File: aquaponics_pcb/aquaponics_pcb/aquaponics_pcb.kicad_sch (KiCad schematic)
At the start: 0 parts

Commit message: initial commit with kicad project
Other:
- added sheet ESP32_MCU (ESP32_MCU.kicad_sch)
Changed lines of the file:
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@@
+		)
+	)
+	(sheet
+		(at 106.68 76.2)
+		(size 29.21 19.05)
+		(exclude_from_sim no)
+		(in_bom yes)
+		(on_board yes)
+		(dnp no)
+		(fields_autoplaced yes)
+		(stroke
+			(width 0.1524)
+			(type solid)
+		)
+		(fill
+			(color 0 0 0 0.0000)
+		)
+		(property "Sheetname" "ESP32_MCU"
+			(at 106.68 75.4884 0)
+			(effects
+				(font
+					(size 1.27 1.27)
+				)
+				(justify left bottom)
+			)
+		)
+		(property "Sheetfile" "ESP32_MCU.kicad_sch"
+			(at 106.68 95.8346 0)
+			(effects
+				(font
+					(size 1.27 1.27)
+				)
+				(justify left top)
+			)
+		)
+		(instances
+			(project "aquaponics_pcb"
+				(path "/c5e5a8d2-0dcc-4520-98a5-511e1dc0d12f"
+					(page "3")
+				)
+			)
 		)
 	)

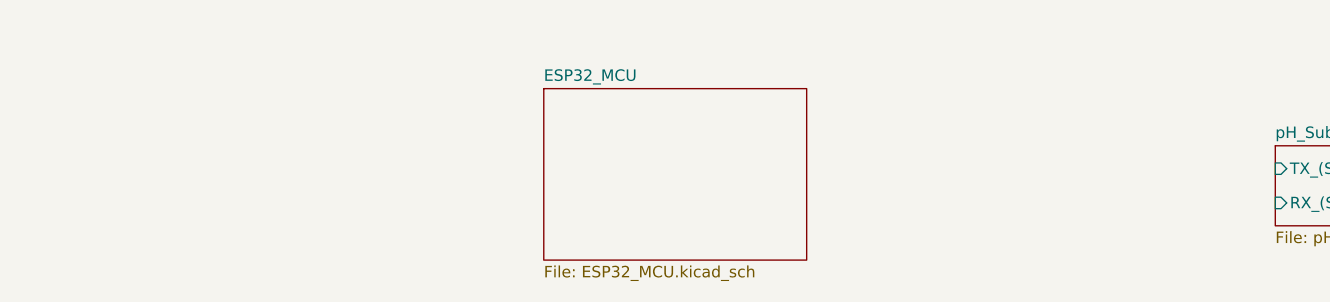
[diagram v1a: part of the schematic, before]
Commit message: finish MCU and start logic isolation block
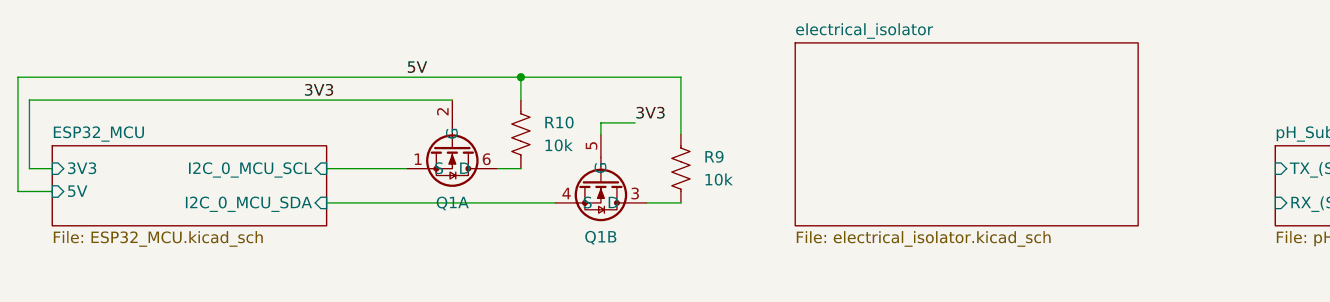
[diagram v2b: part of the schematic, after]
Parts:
- added Q1: SSM6N35AFE,LF, SOTFL50P160X60-6N, symbol SamacSys_Parts:SSM6N35AFE,LF
- added R10, R9: 10k, Resistor_SMD:R_0603_1608Metric_Pad0.98x0.95mm_HandSolder, symbol Device:R_US
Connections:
- new net: Q1.3 (D), R9.1
- new net: Q1.6 (D), R10.1
- new net 3V3: Q1.2 (G), Q1.5 (G)
- new net 5V: R10.2, R9.2
- new net ESP32_MCU/I2C_0_MCU_SCL: Q1.1 (S)
- new net ESP32_MCU/I2C_0_MCU_SDA: Q1.4 (S)
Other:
- added sheet electrical_isolator (electrical_isolator.kicad_sch)
- sheet ESP32_MCU ports: added 3V3, 5V, I2C_0_MCU_SCL, I2C_0_MCU_SDA; removed none

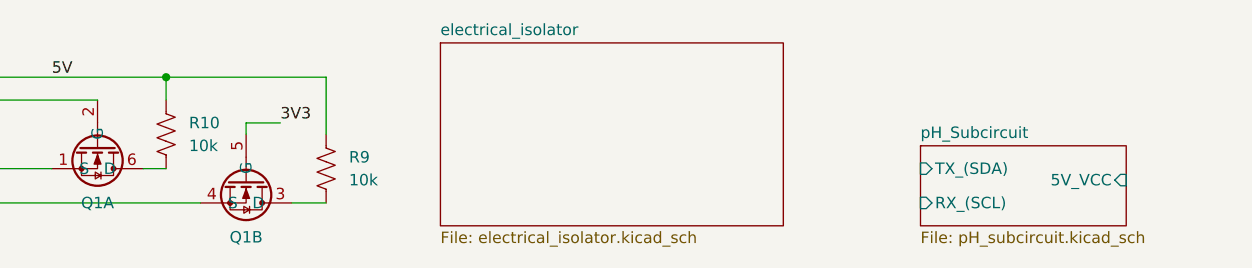
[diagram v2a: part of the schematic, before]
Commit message: update isolator circuit
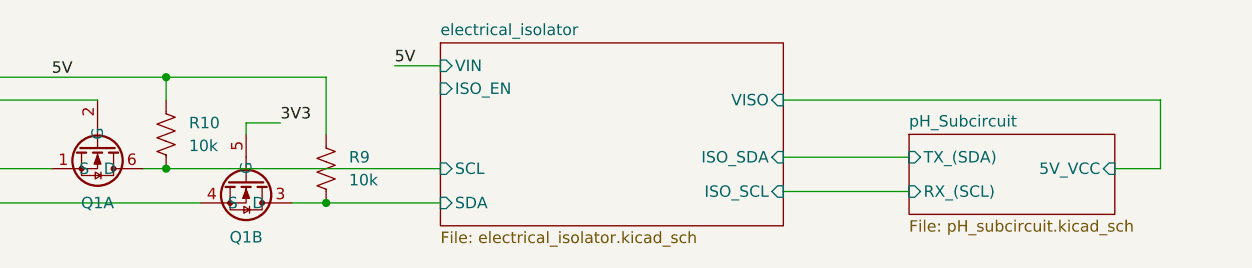
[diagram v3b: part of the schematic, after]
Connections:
- net electrical_isolator/SDA: now reaches Q1.3 (D), R9.1
- net electrical_isolator/SCL: now reaches Q1.6 (D), R10.1
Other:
- sheet electrical_isolator ports: added ISO_EN, ISO_SCL, ISO_SDA, SCL, SDA, VIN, VISO; removed none
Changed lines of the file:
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@@
 	(paper "A4")
+	(junction
+		(at 104.14 85.09)
+		(diameter 0)
+		(color 0 0 0 0)
+	)
+	(junction
+		(at 121.92 88.9)
+		(diameter 0)
+		(color 0 0 0 0)
+	)
 	(junction
 		(at 104.14 74.93)
@@
 	(wire
 		(pts
+			(xy 172.72 83.82) (xy 186.69 83.82)
+		)
+		(stroke
+			(width 0)
+			(type default)
+		)
+	)
+	(wire
+		(pts
+			(xy 172.72 77.47) (xy 214.63 77.47)
+		)
+		(stroke
+			(width 0)
+			(type default)
+		)
+	)
+	(wire
+		(pts
 			(xy 118.11 88.9) (xy 121.92 88.9)
 		)
@@
 	(wire
 		(pts
+			(xy 214.63 77.47) (xy 214.63 85.09)
+		)
+		(stroke
+			(width 0)
+			(type default)
+		)
+	)
+	(wire
+		(pts
+			(xy 214.63 85.09) (xy 209.55 85.09)
+		)
+		(stroke
+			(width 0)
+			(type default)
+		)
+	)
+	(wire
+		(pts
+			(xy 129.54 73.66) (xy 134.62 73.66)
+		)
+		(stroke
+			(width 0)
+			(type default)
+		)
+	)
+	(wire
+		(pts
 			(xy 101.6 85.09) (xy 104.14 85.09)
 		)
@@
 	(wire
 		(pts
+			(xy 104.14 85.09) (xy 134.62 85.09)
+		)
+		(stroke
+			(width 0)
+			(type default)
+		)
+	)
+	(wire
+		(pts
+			(xy 121.92 88.9) (xy 134.62 88.9)
+		)
+		(stroke
+			(width 0)
+			(type default)
+		)
+	)
+	(wire
+		(pts
 			(xy 49.53 77.47) (xy 96.52 77.47)
 		)
@@
 		(pts
 			(xy 104.14 74.93) (xy 104.14 77.47)
+		)
+		(stroke
+			(width 0)
+			(type default)
+		)
+	)
+	(wire
+		(pts
+			(xy 172.72 87.63) (xy 186.69 87.63)
 		)
 		(stroke
@@
 	(label "5V"
 		(at 91.44 74.93 0)
+		(effects
+			(font
+				(size 1.27 1.27)
+			)
+			(justify left bottom)
+		)
+	)
+	(label "5V"
+		(at 129.54 73.66 0)
 		(effects
 			(font
@@
 	)
 	(sheet
-		(at 187.96 82.55)
+		(at 186.69 81.28)
 		(size 22.86 8.89)
 		(exclude_from_sim no)
@@
 		)
 		(property "Sheetname" "pH_Subcircuit"
-			(at 187.96 81.8384 0)
+			(at 186.69 80.5684 0)
 			(effects
 				(font
@@
 		)
 		(property "Sheetfile" "pH_subcircuit.kicad_sch"
-			(at 187.96 92.0246 0)
+			(at 186.69 90.7546 0)
 			(effects
 				(font
@@
 		)
 		(pin "TX_(SDA)" input
-			(at 187.96 85.09 180)
+			(at 186.69 83.82 180)
 			(effects
 				(font
@@
 		)
 		(pin "5V_VCC" input
-			(at 210.82 86.36 0)
+			(at 209.55 85.09 0)
 			(effects
 				(font
@@
 		)
 		(pin "RX_(SCL)" input
-			(at 187.96 88.9 180)
+			(at 186.69 87.63 180)
 			(effects
 				(font
@@
 			)
 		)
+		(pin "SDA" input
+			(at 134.62 88.9 180)
+			(effects
+				(font
+					(size 1.27 1.27)
+				)
+				(justify left)
+			)
+		)
+		(pin "ISO_SCL" input
+			(at 172.72 87.63 0)
+			(effects
+				(font
+					(size 1.27 1.27)
+				)
+				(justify right)
+			)
+		)
+		(pin "ISO_EN" input
+			(at 134.62 76.2 180)
+			(effects
+				(font
+					(size 1.27 1.27)
+				)
+				(justify left)
+			)
+		)
+		(pin "VISO" input
+			(at 172.72 77.47 0)
+			(effects
+				(font
+					(size 1.27 1.27)
+				)
+				(justify right)
+			)
+		)
+		(pin "ISO_SDA" input
+			(at 172.72 83.82 0)
+			(effects
+				(font
+					(size 1.27 1.27)
+				)
+				(justify right)
+			)
+		)
+		(pin "SCL" input
+			(at 134.62 85.09 180)
+			(effects
+				(font
+					(size 1.27 1.27)
+				)
+				(justify left)
+			)
+		)
+		(pin "VIN" input
+			(at 134.62 73.66 180)
+			(effects
+				(font
+					(size 1.27 1.27)
+				)
+				(justify left)
+			)
+		)

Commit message: begin motor control sch
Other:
- added sheet Cond_Subcircuit (pH_subcircuit.kicad_sch)
- added sheet DO_Subcircuit (pH_subcircuit.kicad_sch)
- added sheet Motor_Control_1 (motor_control_1.kicad_sch)

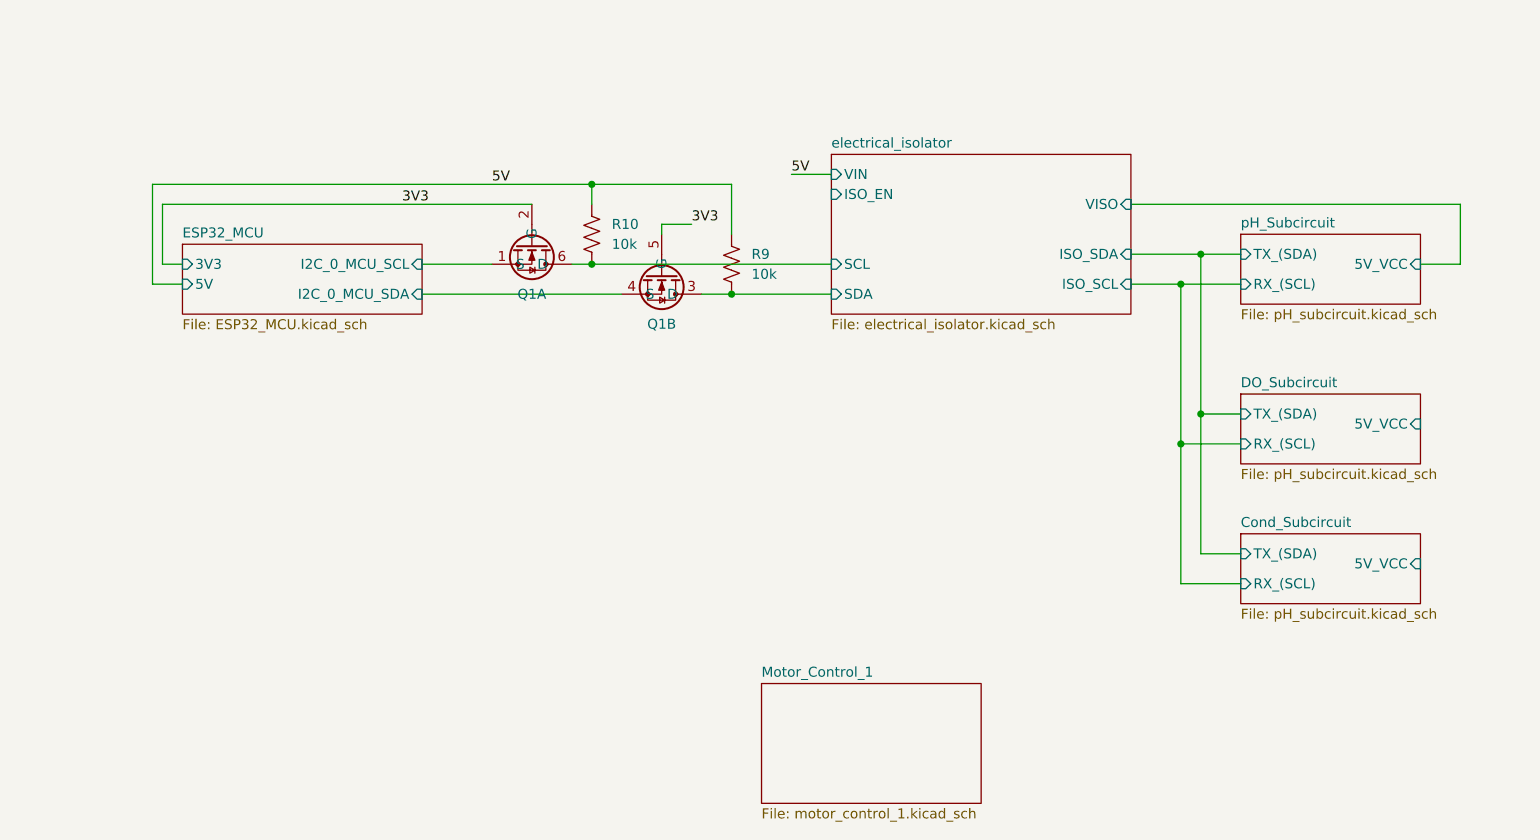
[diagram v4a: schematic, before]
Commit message: add ezo datasheets, update motor schematic and add 2 motors
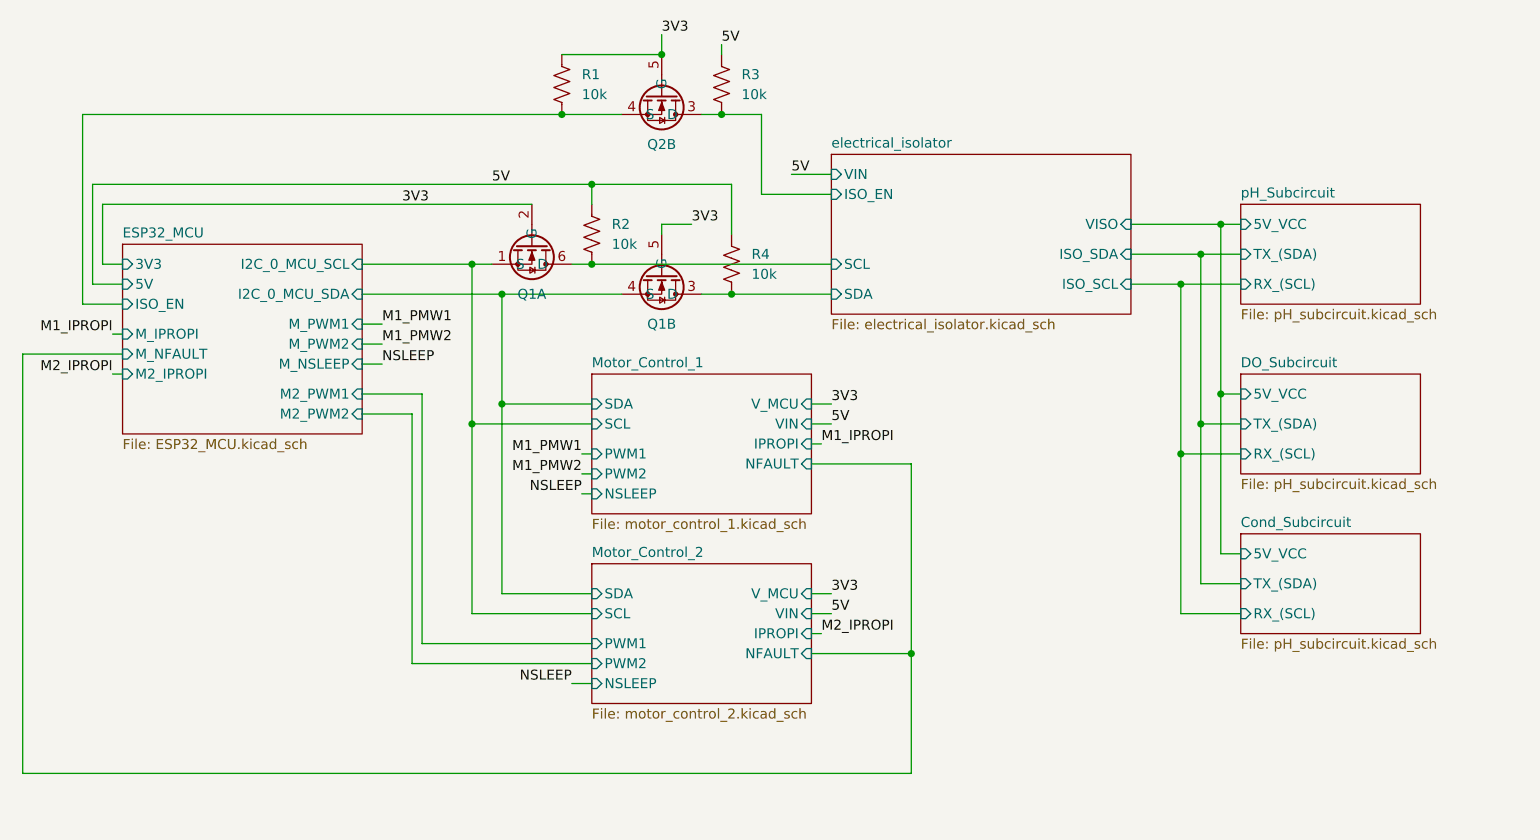
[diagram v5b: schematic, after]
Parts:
- added Q2: SSM6N35AFE,LF, SOTFL50P160X60-6N, symbol SamacSys_Parts:SSM6N35AFE,LF
- added R1, R3: 10k, Resistor_SMD:R_0603_1608Metric_Pad0.98x0.95mm_HandSolder, symbol Device:R_US
- renumbered R10 to R2, R9 to R4
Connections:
- net 3V3: now also Q2.5 (G), R1.2
- net 5V: now also R3.2
- net electrical_isolator/ISO_EN: now also Q2.3 (D), R3.1
- new net ESP32_MCU/ISO_EN: Q2.4 (S), R1.1
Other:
- added sheet Motor_Control_2 (motor_control_2.kicad_sch)
- sheet ESP32_MCU ports: added ISO_EN, M2_IPROPI, M2_PWM1, M2_PWM2, M_IPROPI, M_NFAULT, M_NSLEEP, M_PWM1, M_PWM2; removed none
- sheet Motor_Control_1 ports: added IPROPI, NFAULT, NSLEEP, PWM1, PWM2, SCL, SDA, VIN, V_MCU; removed none

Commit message: add initial pcb layout
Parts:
- Q1, Q2: footprint SOTFL50P160X60-6N -> SamacSys_Parts:SOTFL50P160X60-6N
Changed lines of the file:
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@@
 			)
 		)
-		(property "Footprint" "SOTFL50P160X60-6N"
+		(property "Footprint" "SamacSys_Parts:SOTFL50P160X60-6N"
 			(at 18.11 99.06 0)
 			(effects
@@
 			)
 		)
-		(property "Footprint" "SOTFL50P160X60-6N"
+		(property "Footprint" "SamacSys_Parts:SOTFL50P160X60-6N"
 			(at 1.6 118.11 0)
 			(effects
@@
 			)
 		)
-		(property "Footprint" "SOTFL50P160X60-6N"
+		(property "Footprint" "SamacSys_Parts:SOTFL50P160X60-6N"
 			(at 18.11 121.92 0)
 			(effects

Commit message: finish ground and power pours. fix rules and run final DRC. export gerbers
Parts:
- R1, R2, R3, R4: JLCPCB Part # (none) -> C98220; LCSC Part Number (none) -> C98220
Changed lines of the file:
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@@
+			)
+		)
+		(property "LCSC Part Number" "C98220"
+			(at 120.65 62.23 0)
+			(effects
+				(font
+					(size 1.27 1.27)
+				)
+				(hide yes)
+			)
+		)
+		(property "JLCPCB Part #" "C98220"
+			(at 120.65 62.23 0)
+			(effects
+				(font
+					(size 1.27 1.27)
+				)
+				(hide yes)
 			)
 		)
@@
 			)
 		)
+		(property "LCSC Part Number" "C98220"
+			(at 121.92 85.09 0)
+			(effects
+				(font
+					(size 1.27 1.27)
+				)
+				(hide yes)
+			)
+		)
+		(property "JLCPCB Part #" "C98220"
+			(at 121.92 85.09 0)
+			(effects
+				(font
+					(size 1.27 1.27)
+				)
+				(hide yes)
+			)
+		)
 		(pin "1"
 		)
@@
 				)
 				(justify left top)
+				(hide yes)
+			)
+		)
+		(property "LCSC Part Number" ""
+			(at 113.03 64.77 90)
+			(effects
+				(font
+					(size 1.27 1.27)
+				)
+				(hide yes)
+			)
+		)
+		(property "JLCPCB Part #" ""
+			(at 113.03 64.77 90)
+			(effects
+				(font
+					(size 1.27 1.27)
+				)
 				(hide yes)
 			)
@@
 			)
 		)
+		(property "LCSC Part Number" ""
+			(at 96.52 83.82 90)
+			(effects
+				(font
+					(size 1.27 1.27)
+				)
+				(hide yes)
+			)
+		)
+		(property "JLCPCB Part #" ""
+			(at 96.52 83.82 90)
+			(effects
+				(font
+					(size 1.27 1.27)
+				)
+				(hide yes)
+			)
+		)
 		(pin "3"
 		)
@@
 			)
 		)
+		(property "LCSC Part Number" ""
+			(at 113.03 87.63 90)
+			(effects
+				(font
+					(size 1.27 1.27)
+				)
+				(hide yes)
+			)
+		)
+		(property "JLCPCB Part #" ""
+			(at 113.03 87.63 90)
+			(effects
+				(font
+					(size 1.27 1.27)
+				)
+				(hide yes)
+			)
+		)
 		(pin "3"
 		)
@@
 			)
 		)
+		(property "LCSC Part Number" "C98220"
+			(at 104.14 81.28 0)
+			(effects
+				(font
+					(size 1.27 1.27)
+				)
+				(hide yes)
+			)
+		)
+		(property "JLCPCB Part #" "C98220"
+			(at 104.14 81.28 0)
+			(effects
+				(font
+					(size 1.27 1.27)
+				)
+				(hide yes)
+			)
+		)
 		(pin "1"
 		)
@@
 			(at 100.33 62.23 0)
 			(effects
+				(font
+					(size 1.27 1.27)
+				)
+				(hide yes)
+			)
+		)
+		(property "LCSC Part Number" "C98220"
+			(at 100.33 62.23 0)
+			(effects
+				(font
+					(size 1.27 1.27)
+				)
+				(hide yes)
+			)
+		)
+		(property "JLCPCB Part #" "C98220"
+			(at 100.33 62.23 0)
+			(effects
